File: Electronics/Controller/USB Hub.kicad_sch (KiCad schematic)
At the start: 45 parts, among them J16 MASTER TABLET, J17 292303-7, J18 292303-7, U16 USB2517, U17 MIC2026-1YM, Y1 FA-238 24.0000MD30X-W5

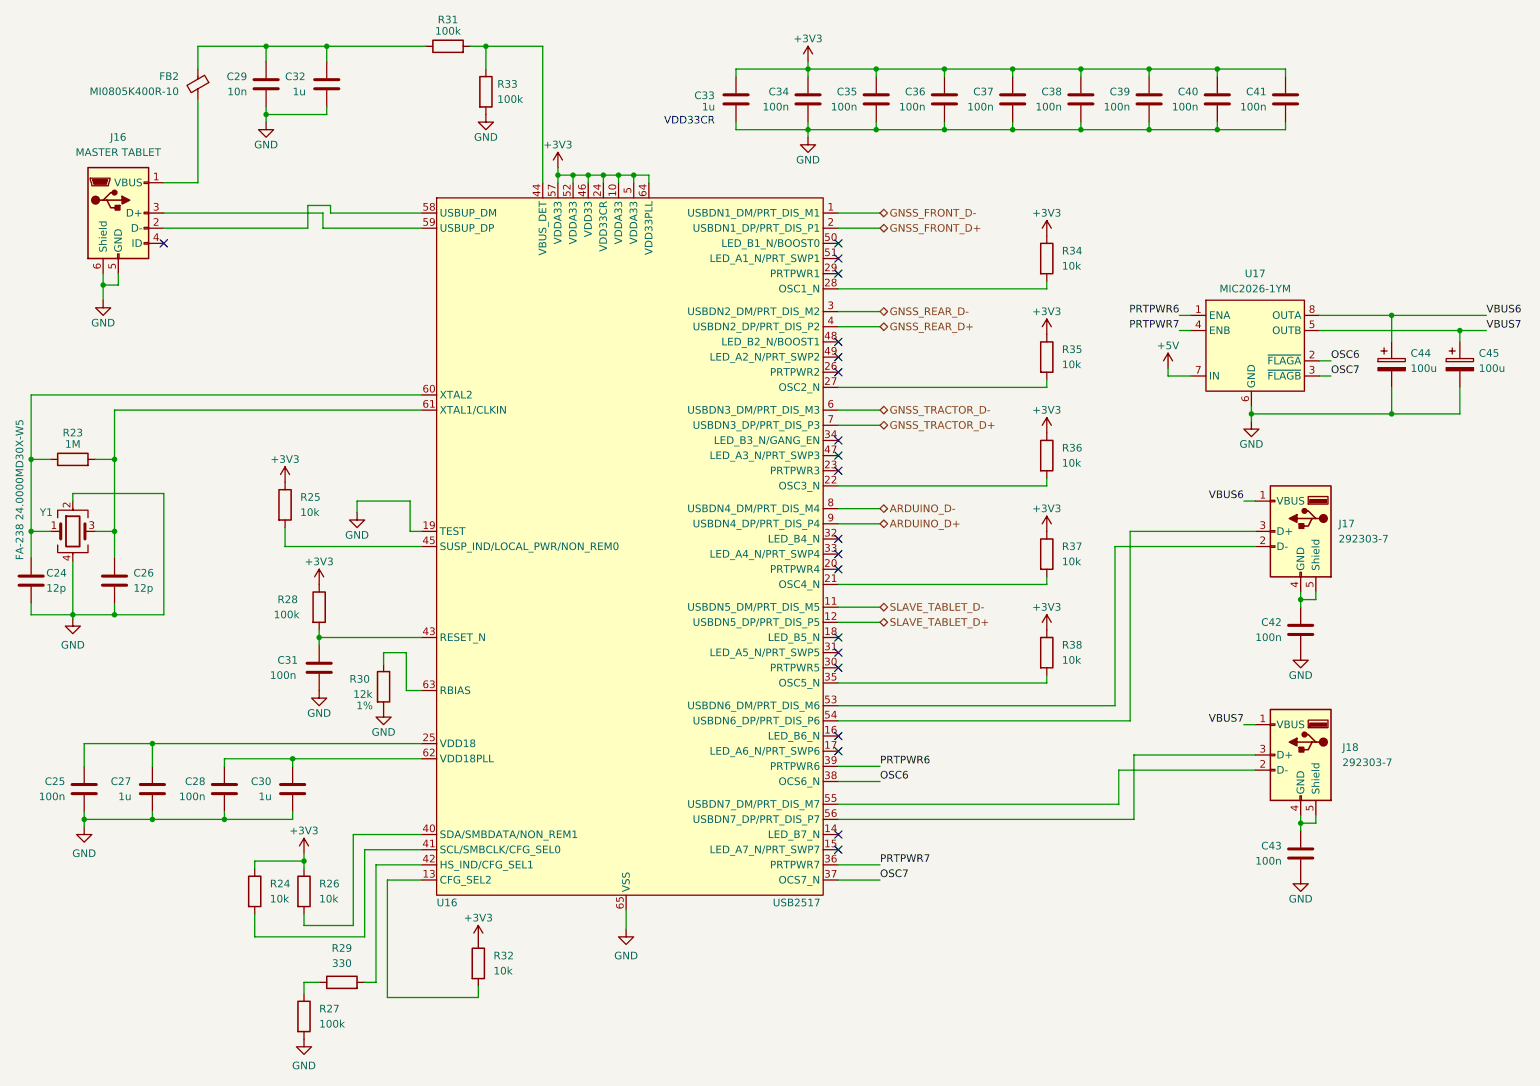
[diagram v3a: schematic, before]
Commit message: Changed switches and lamps. Removed status LEDs. Working on PCB layout.
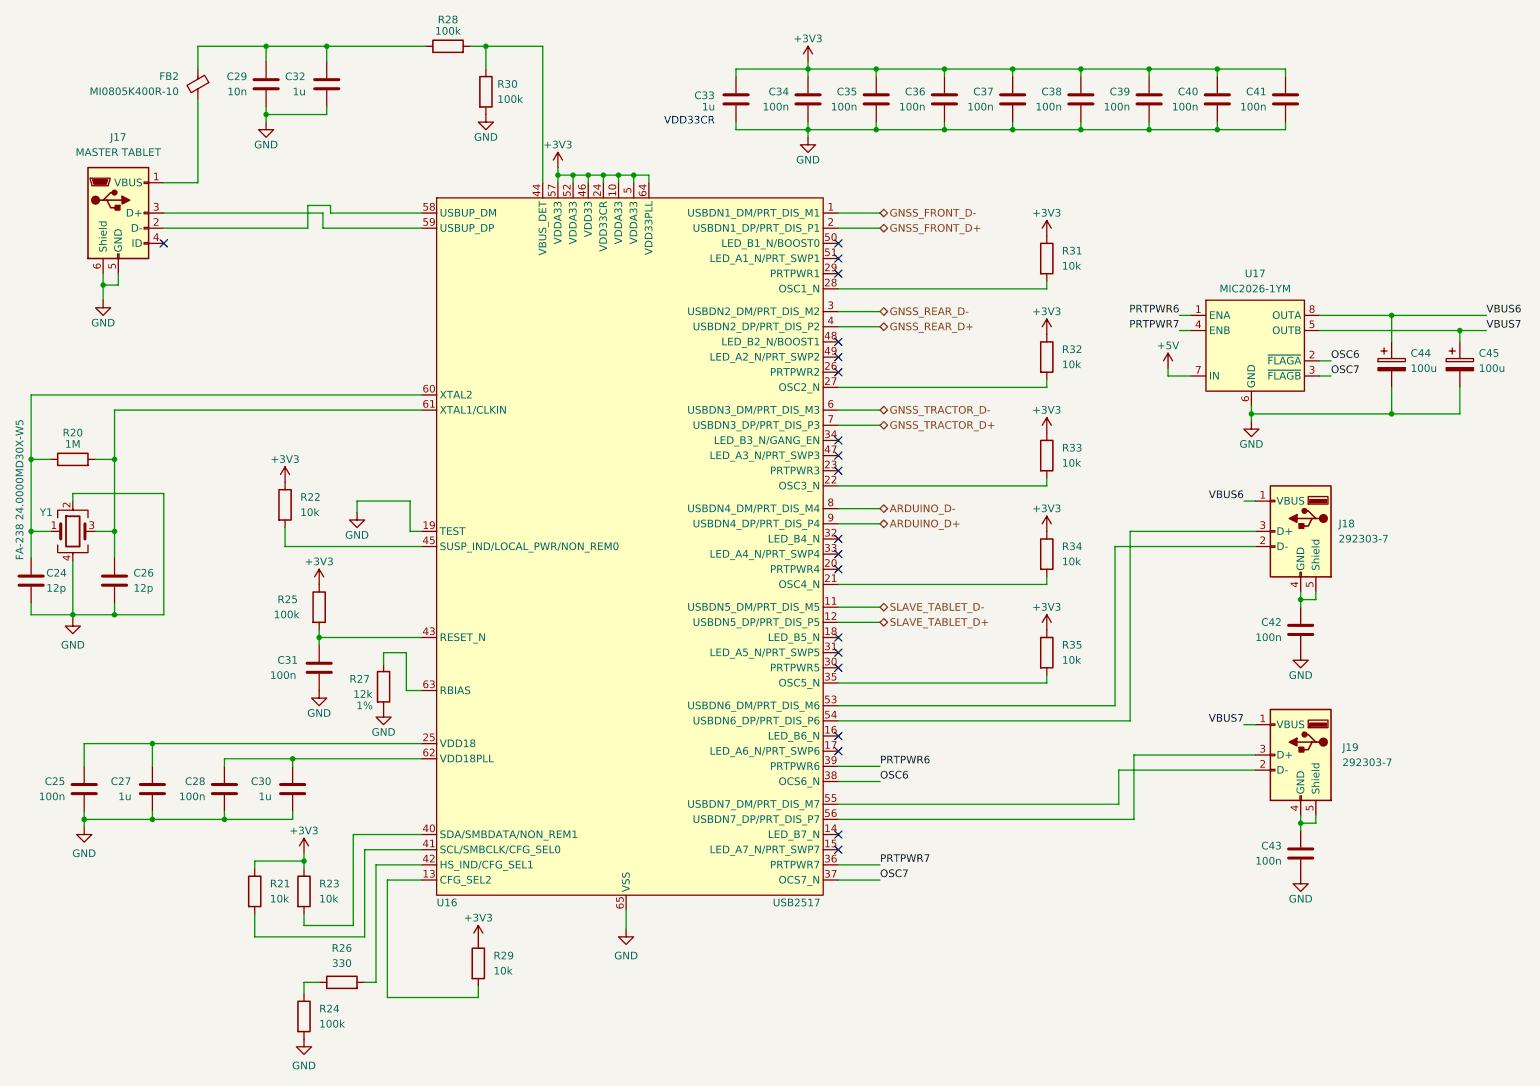
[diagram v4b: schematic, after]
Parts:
- renumbered J16 to J17, J17 to J18, J18 to J19, R23 to R20, R24 to R21, R25 to R22, R26 to R23, R27 to R24, R28 to R25, R29 to R26, R30 to R27, R31 to R28, R32 to R29, R33 to R30, R34 to R31, R35 to R32, R36 to R33, R37 to R34, R38 to R35

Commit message: Added 4.7uF caps to FT232RL on controller.
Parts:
- C24, C26: LCSC (none) -> C1792
- C25, C28, C31, C34, C35, C36, C37, C38, C39, C40, C41, C42, C43: LCSC (none) -> C1711
- C27, C30, C32, C33: LCSC (none) -> C24123
- C29: LCSC (none) -> C1710
- C44, C45: LCSC (none) -> C340733
- J17: LCSC (none) -> C428495
- R20: LCSC (none) -> C17514
- R21, R22, R23, R29, R31, R32, R33, R34, R35: LCSC (none) -> C17414
- R24, R25, R28, R30: LCSC (none) -> C17407
- R26: LCSC (none) -> C17630
- R27: LCSC (none) -> C17444
- U16: LCSC (none) -> C1521556
- U17: LCSC (none) -> C144190
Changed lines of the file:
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@@
   (title_block
     (title "Tandem Leveller Controller")
-    (date "2025-02-22")
+    (date "2025-03-11")
     (rev "V1.0")
     (company "(C) andy@britishideas.com 2025")
@@
       (effects (font (size 1.27 1.27)) hide)
     )
+    (property "LCSC" "C17514" (at 36.195 88.265 0)
+      (effects (font (size 1.27 1.27)) hide)
+    )
     (pin "1")
     (pin "2")
@@
       (effects (font (size 1.27 1.27)))
     )
+    (property "LCSC" "C17444" (at 88.265 126.365 0)
+      (effects (font (size 1.27 1.27)) hide)
+    )
     (pin "1")
     (pin "2")
@@
     )
     (property "manf#" "MI0805K400R-10" (at 57.15 25.4 0)
+      (effects (font (size 1.27 1.27)) hide)
+    )
+    (property "LCSC" "" (at 57.15 25.4 0)
       (effects (font (size 1.27 1.27)) hide)
     )
@@
       (effects (font (size 1.27 1.27)) hide)
     )
+    (property "LCSC" "C24123" (at 78.74 25.4 0)
+      (effects (font (size 1.27 1.27)) hide)
+    )
     (pin "1")
     (pin "2")
@@
       (effects (font (size 1.27 1.27)) hide)
     )
+    (property "LCSC" "C1711" (at 159.385 27.94 0)
+      (effects (font (size 1.27 1.27)) hide)
+    )
     (pin "1")
     (pin "2")
@@
       (effects (font (size 1.27 1.27)) hide)
     )
+    (property "LCSC" "C1711" (at 239.395 27.94 0)
+      (effects (font (size 1.27 1.27)) hide)
+    )
     (pin "1")
     (pin "2")
@@
       (effects (font (size 1.27 1.27)) hide)
     )
+    (property "LCSC" "C17414" (at 74.93 160.655 0)
+      (effects (font (size 1.27 1.27)) hide)
+    )
     (pin "1")
     (pin "2")
@@
       (effects (font (size 1.27 1.27)) hide)
     )
+    (property "LCSC" "C17414" (at 199.39 54.61 0)
+      (effects (font (size 1.27 1.27)) hide)
+    )
     (pin "1")
     (pin "2")
@@
       (effects (font (size 1.27 1.27)) hide)
     )
+    (property "LCSC" "C1711" (at 241.935 154.305 0)
+      (effects (font (size 1.27 1.27)) hide)
+    )
     (pin "1")
     (pin "2")
@@
       (effects (font (size 1.27 1.27)) hide)
     )
+    (property "LCSC" "C340733" (at 268.605 72.39 0)
+      (effects (font (size 1.27 1.27)) hide)
+    )
     (pin "2")
     (pin "1")
@@
       (effects (font (size 1.27 1.27)) hide)
     )
+    (property "LCSC" "C1711" (at 227.965 27.94 0)
+      (effects (font (size 1.27 1.27)) hide)
+    )
     (pin "1")
     (pin "2")
@@
       (effects (font (size 1.27 1.27)) hide)
     )
+    (property "LCSC" "C17414" (at 71.755 95.885 0)
+      (effects (font (size 1.27 1.27)) hide)
+    )
     (pin "1")
     (pin "2")
@@
       (effects (font (size 1.27 1.27)) hide)
     )
+    (property "LCSC" "C1711" (at 38.1 143.51 0)
+      (effects (font (size 1.27 1.27)) hide)
+    )
     (pin "1")
     (pin "2")
@@
     )
     (property "manf#" "10103594-0001LF" (at 43.815 46.99 0)
+      (effects (font (size 1.27 1.27)) hide)
+    )
+    (property "LCSC" "C428495" (at 43.815 46.99 0)
       (effects (font (size 1.27 1.27)) hide)
     )
@@
       (effects (font (size 1.27 1.27)) hide)
     )
+    (property "LCSC" "C1792" (at 29.21 108.585 0)
+      (effects (font (size 1.27 1.27)) hide)
+    )
     (pin "1")
     (pin "2")
@@
       (effects (font (size 1.27 1.27)) hide)
     )
+    (property "LCSC" "C1711" (at 193.675 27.94 0)
+      (effects (font (size 1.27 1.27)) hide)
+    )
     (pin "1")
     (pin "2")
@@
     )
     (property "Datasheet" "~" (at 43.18 108.585 0)
+      (effects (font (size 1.27 1.27)) hide)
+    )
+    (property "LCSC" "C1792" (at 43.18 108.585 0)
       (effects (font (size 1.27 1.27)) hide)
     )
@@
       (effects (font (size 1.27 1.27)) hide)
     )
+    (property "LCSC" "C24123" (at 147.32 27.94 0)
+      (effects (font (size 1.27 1.27)) hide)
+    )
     (pin "1")
     (pin "2")
@@
     )
     (property "Datasheet" " ~" (at 238.125 139.065 0)
+      (effects (font (size 1.27 1.27)) hide)
+    )
+    (property "LCSC" "" (at 241.935 137.795 0)
       (effects (font (size 1.27 1.27)) hide)
     )
@@
       (effects (font (size 1.27 1.27)) hide)
     )
+    (property "LCSC" "C17414" (at 199.39 87.63 0)
+      (effects (font (size 1.27 1.27)) hide)
+    )
     (pin "1")
     (pin "2")
@@
       (effects (font (size 1.27 1.27)) hide)
     )
+    (property "LCSC" "C24123" (at 73.025 143.51 0)
+      (effects (font (size 1.27 1.27)) hide)
+    )
     (pin "1")
     (pin "2")
@@
       (effects (font (size 1.27 1.27)) hide)
     )
+    (property "LCSC" "C1711" (at 205.105 27.94 0)
+      (effects (font (size 1.27 1.27)) hide)
+    )
     (pin "1")
     (pin "2")
@@
     )
     (property "Datasheet" "" (at 226.06 76.835 0)
+      (effects (font (size 1.27 1.27)) hide)
+    )
+    (property "LCSC" "C144190" (at 226.06 76.835 0)
       (effects (font (size 1.27 1.27)) hide)
     )
@@
       (effects (font (size 1.27 1.27)) hide)
     )
+    (property "LCSC" "C1710" (at 68.58 25.4 0)
+      (effects (font (size 1.27 1.27)) hide)
+    )
     (pin "1")
     (pin "2")
@@
       (effects (font (size 1.27 1.27)) hide)
     )
+    (property "LCSC" "C17414" (at 199.39 71.12 0)
+      (effects (font (size 1.27 1.27)) hide)
+    )
     (pin "1")
     (pin "2")
@@
       (effects (font (size 1.27 1.27)) hide)
     )
+    (property "LCSC" "C17414" (at 199.39 104.14 0)
+      (effects (font (size 1.27 1.27)) hide)
+    )
     (pin "1")
     (pin "2")
@@
       (effects (font (size 1.27 1.27)) hide)
     )
+    (property "LCSC" "C17407" (at 105.41 26.67 0)
+      (effects (font (size 1.27 1.27)) hide)
+    )
     (pin "1")
     (pin "2")
@@
       (effects (font (size 1.27 1.27)) hide)
     )
+    (property "LCSC" "C17414" (at 104.14 172.72 0)
+      (effects (font (size 1.27 1.27)) hide)
+    )
     (pin "1")
     (pin "2")
@@
       (effects (font (size 1.27 1.27)) hide)
     )
+    (property "LCSC" "C17414" (at 66.675 160.655 0)
+      (effects (font (size 1.27 1.27)) hide)
+    )
     (pin "1")
     (pin "2")
@@
     )
     (property "Datasheet" "~" (at 81.28 175.895 0)
+      (effects (font (size 1.27 1.27)) hide)
+    )
+    (property "LCSC" "C17630" (at 81.28 175.895 0)
       (effects (font (size 1.27 1.27)) hide)
     )
@@
       (effects (font (size 1.27 1.27)) hide)
     )
+    (property "LCSC" "C1711" (at 77.47 123.19 0)
+      (effects (font (size 1.27 1.27)) hide)
+    )
     (pin "1")
     (pin "2")
@@
     )
     (property "manf#" "FA-238V 12.0000MB-W3" (at 36.195 100.33 0)
+      (effects (font (size 1.27 1.27)) hide)
+    )
+    (property "LCSC" "" (at 36.195 100.33 0)
       (effects (font (size 1.27 1.27)) hide)
     )
@@
       (effects (font (size 1.27 1.27)) hide)
     )
+    (property "LCSC" "C1711" (at 216.535 27.94 0)
+      (effects (font (size 1.27 1.27)) hide)
+    )
     (pin "1")
     (pin "2")
@@
       (effects (font (size 1.27 1.27)) hide)
     )
+    (property "LCSC" "C1711" (at 182.245 27.94 0)
+      (effects (font (size 1.27 1.27)) hide)
+    )
     (pin "1")
     (pin "2")
@@
       (effects (font (size 1.27 1.27)) hide)
     )
+    (property "LCSC" "C1711" (at 61.595 143.51 0)
+      (effects (font (size 1.27 1.27)) hide)
+    )
     (pin "1")
     (pin "2")
@@
     )
     (property "Datasheet" "" (at 164.465 46.99 0)
+      (effects (font (size 1.27 1.27)) hide)
+    )
+    (property "LCSC" "C1521556" (at 178.435 120.65 0)
       (effects (font (size 1.27 1.27)) hide)
     )
@@
       (effects (font (size 1.27 1.27)) hide)
     )
+    (property "LCSC" "C1711" (at 241.935 116.84 0)
+      (effects (font (size 1.27 1.27)) hide)
+    )
     (pin "1")
     (pin "2")
@@
     )
     (property "Datasheet" " ~" (at 238.125 101.6 0)
+      (effects (font (size 1.27 1.27)) hide)
+    )
+    (property "LCSC" "" (at 241.935 100.33 0)
       (effects (font (size 1.27 1.27)) hide)
     )
@@
       (effects (font (size 1.27 1.27)) hide)
     )
+    (property "LCSC" "C340733" (at 257.175 72.39 0)
+      (effects (font (size 1.27 1.27)) hide)
+    )
     (pin "2")
     (pin "1")
@@
       (effects (font (size 1.27 1.27)) hide)
     )
+    (property "LCSC" "C24123" (at 49.53 143.51 0)
+      (effects (font (size 1.27 1.27)) hide)
+    )
     (pin "1")
     (pin "2")
@@
       (effects (font (size 1.27 1.27)) hide)
     )
+    (property "LCSC" "C17407" (at 74.93 181.61 0)
+      (effects (font (size 1.27 1.27)) hide)
+    )
     (pin "1")
     (pin "2")
@@
       (effects (font (size 1.27 1.27)) hide)
     )
+    (property "LCSC" "C1711" (at 170.815 27.94 0)
+      (effects (font (size 1.27 1.27)) hide)
+    )
     (pin "1")
     (pin "2")
@@
       (effects (font (size 1.27 1.27)) hide)
     )
+    (property "LCSC" "C17407" (at 77.47 113.03 0)
+      (effects (font (size 1.27 1.27)) hide)
+    )
     (pin "1")
     (pin "2")
@@
       (effects (font (size 1.27 1.27)) hide)
     )
+    (property "LCSC" "C17407" (at 99.06 19.05 0)
+      (effects (font (size 1.27 1.27)) hide)
+    )
     (pin "1")
     (pin "2")
@@
       (effects (font (size 1.27 1.27)) hide)
     )
+    (property "LCSC" "C17414" (at 199.39 120.65 0)
+      (effects (font (size 1.27 1.27)) hide)
+    )
